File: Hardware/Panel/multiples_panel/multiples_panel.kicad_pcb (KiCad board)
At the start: 2 copper layers, 50 x 200 mm, 16 parts

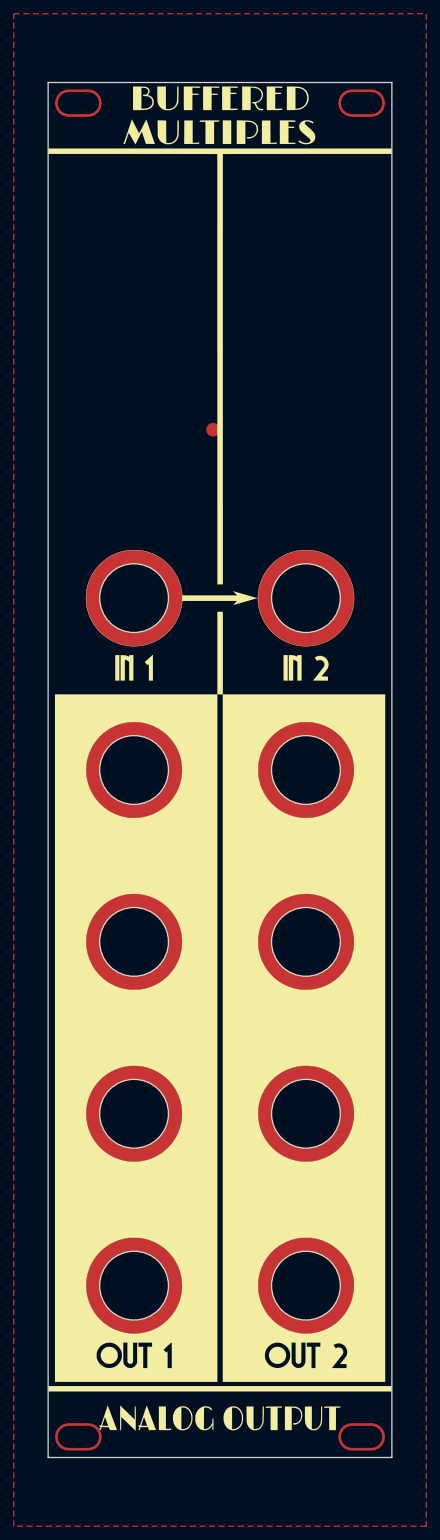
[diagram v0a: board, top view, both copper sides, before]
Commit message: No NPTH specialization
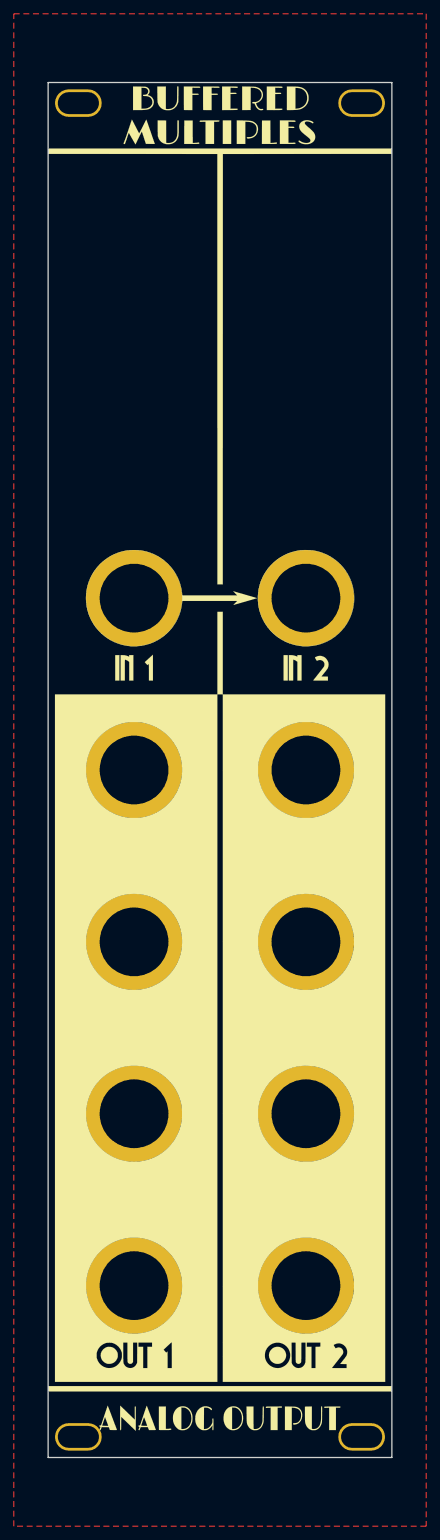
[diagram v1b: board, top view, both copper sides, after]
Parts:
- removed GP1: Ground_point_for_NPTH, Kosmo_panel:Ground_point_for_NPTH
- H1, H10, H11, H12, H2, H4, H5, H7, H8, H9: footprint Kosmo_panel:Kosmo_Jack_Hole_NPTH -> Kosmo_panel:Kosmo_Jack_Hole
- H3, H6: footprint Kosmo_panel:Kosmo_Panel_Dual_Slotted_Mounting_Holes_NPTH -> Kosmo_panel:Kosmo_Panel_Dual_Slotted_Mounting_Holes
